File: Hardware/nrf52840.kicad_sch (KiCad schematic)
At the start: 15 parts, among them J1 Conn_01x01_Pad, J2 Conn_01x01_Pad, J3 Conn_01x02_Pin, J4 Conn_01x07_Pad, J5 Conn_01x07_Pad, J6 Conn_01x01_Pad, SW1 PCM12SMTR, SW2 D2LS-21, SW3 D2LS-21, SW4 D2LS-21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

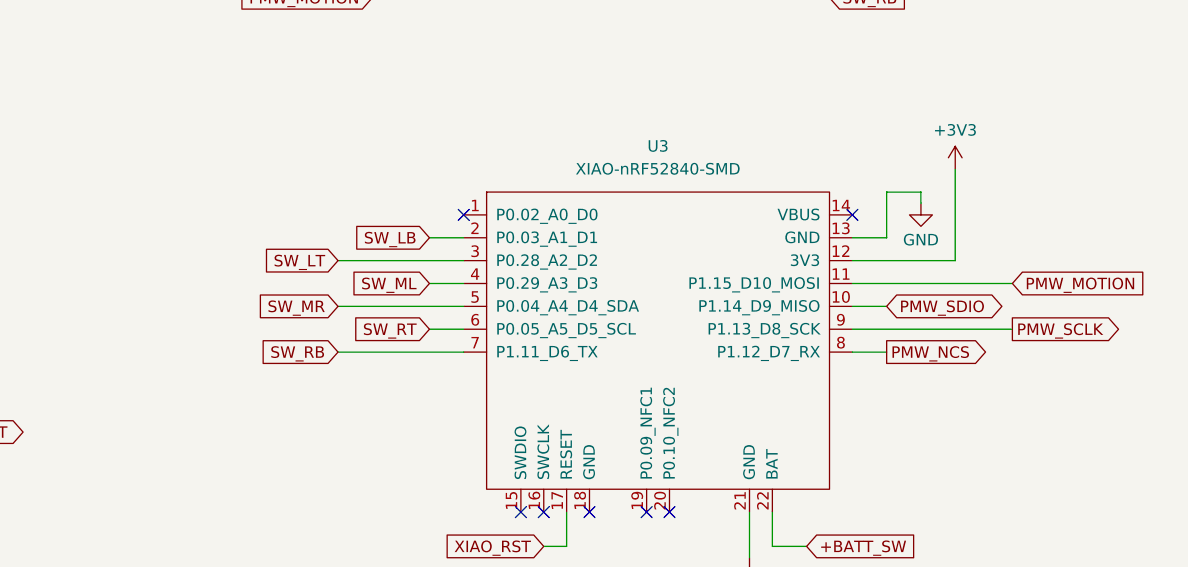
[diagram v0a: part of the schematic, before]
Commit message: nrf52840.kicad_sch: update the connections of the (not real) U3 symbol
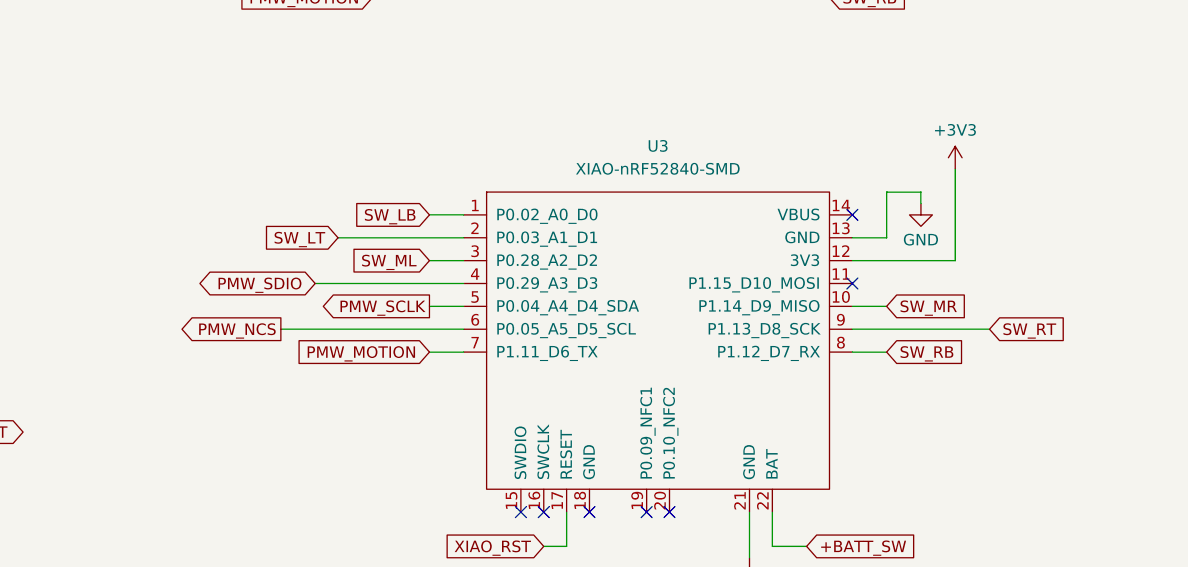
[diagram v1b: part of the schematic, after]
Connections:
- net PMW_MOTION: now also U3.7 (P1.11_D6_TX); no longer U3.11 (P1.15_D10_MOSI)
- net PMW_NCS: now also U3.6 (P0.05_A5_D5_SCL); no longer U3.8 (P1.12_D7_RX)
- net PMW_SCLK: now also U3.5 (P0.04_A4_D4_SDA); no longer U3.9 (P1.13_D8_SCK)
- net PMW_SDIO: now also U3.4 (P0.29_A3_D3); no longer U3.10 (P1.14_D9_MISO)
- net SW_LB: now also U3.1 (P0.02_A0_D0); no longer U3.2 (P0.03_A1_D1)
- net SW_LT: now also U3.2 (P0.03_A1_D1); no longer U3.3 (P0.28_A2_D2)
- net SW_ML: now also U3.3 (P0.28_A2_D2); no longer U3.4 (P0.29_A3_D3)
- net SW_MR: now also U3.10 (P1.14_D9_MISO); no longer U3.5 (P0.04_A4_D4_SDA)
- net SW_RB: now also U3.8 (P1.12_D7_RX); no longer U3.7 (P1.11_D6_TX)
- net SW_RT: now also U3.9 (P1.13_D8_SCK); no longer U3.6 (P0.05_A5_D5_SCL)
